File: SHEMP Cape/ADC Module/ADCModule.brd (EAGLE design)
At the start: 48.9 x 67.6 mm, 51 parts, among them U1 ADS8568_PM_64, U2 LP2950-3.3ACZ

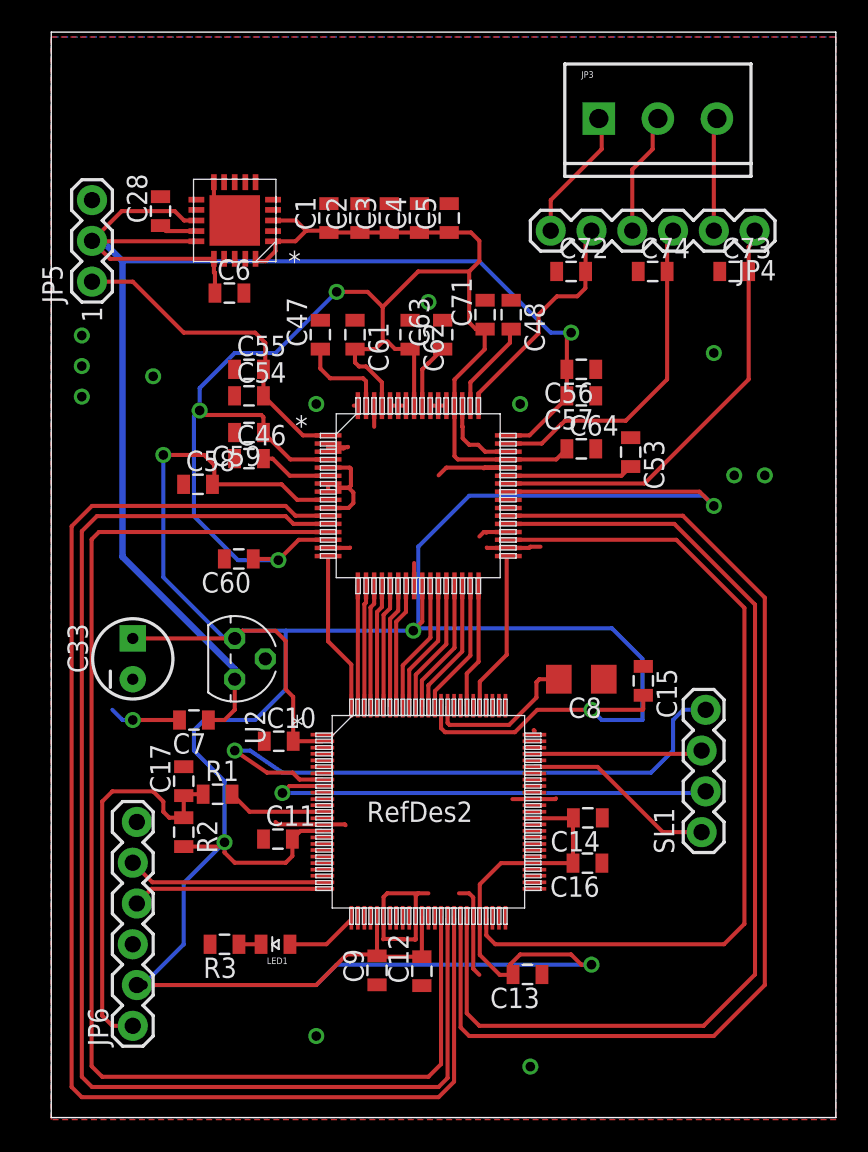
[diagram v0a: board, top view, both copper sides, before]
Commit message: Changed the ADC Module board for boardrouter considerations.
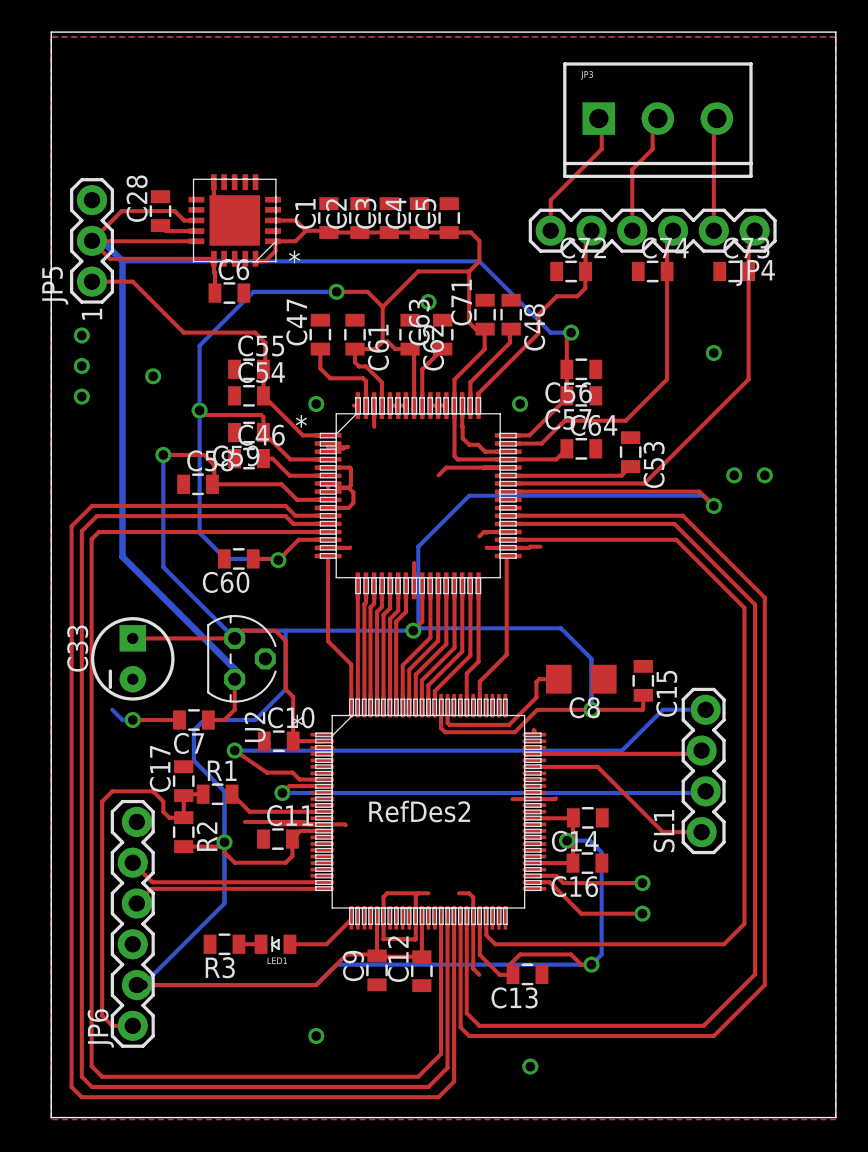
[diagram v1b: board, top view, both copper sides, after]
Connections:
- new net RX1A: U$1.52
- new net TX1A: U$1.53
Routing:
- net RX1A: track 0.00 -> 7.54 mm, vias 0 -> 1
- net TX1A: track 0.00 -> 6.92 mm, vias 0 -> 1
- net GND: track 66.2 -> 71.1 mm
- net VDD3V3_D: track 252.0 -> 248.5 mm, vias 7 -> 8
- net SS: track 38.6 -> 36.5 mm
- net VDD5V0_A: track 104.8 -> 106.4 mm

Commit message: Added new gerbers for boardrouter.
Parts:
- removed JP3: M03SCREW_LOCK, ASL:SCREWTERMINAL-3.5MM-3_LOCK.007S
- added JP1: M03-SCREW-5MM, ASL:SCREWTERMINAL-5MM-3
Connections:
- net N$1: now also JP1.3; no longer JP3.3
- net N$2: now also JP1.2; no longer JP3.2
- net N$3: now also JP1.1; no longer JP3.1
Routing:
- net N$1: track 7.06 -> 8.08 mm
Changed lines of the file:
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@@
 <?xml version="1.0" encoding="utf-8"?>
 <!DOCTYPE eagle SYSTEM "eagle.dtd">
-<eagle version="6.4">
+<eagle version="6.5.0">
 <drawing>
 <settings>
@@
 <element name="C6" library="SensorCape" package="0805" value="10uF" x="11.0998" y="50.0888"/>
 <element name="C7" library="SensorCape" package="0805" value="10uF" x="8.89" y="23.495" rot="R180"/>
-<element name="JP3" library="ASL" package="SCREWTERMINAL-3.5MM-3_LOCK.007S" value="M03SCREW_LOCK" x="34.29" y="60.96"/>
 <element name="JP4" library="ASL" package="1X06" value="" x="37.465" y="53.975" rot="R180"/>
 <element name="U2" library="ASL" package="TO92" value="LP2950-3.3ACZ" x="11.43" y="27.305" rot="R270"/>
@@
 <element name="LED1" library="ASL" package="LED-0805" value="" x="13.97" y="9.525" rot="R180"/>
 <element name="R3" library="SensorCape" package="0805" value="" x="10.795" y="9.525" rot="R180"/>
+<element name="JP1" library="ASL" package="SCREWTERMINAL-5MM-3" value="M03-SCREW-5MM" x="32.385" y="61.595"/>
 </elements>
 <signals>
@@
 </signal>
 <signal name="N$1">
-<contactref element="JP3" pad="3"/>
 <contactref element="JP4" pad="2"/>
-<wire x1="41.275" y1="53.975" x2="41.275" y2="60.7672" width="0.254" layer="1"/>
-<wire x1="41.275" y1="60.7672" x2="41.4678" y2="60.96" width="0.254" layer="1"/>
+<contactref element="JP1" pad="3"/>
+<wire x1="41.275" y1="53.975" x2="41.275" y2="60.485" width="0.4064" layer="16"/>
+<wire x1="41.275" y1="60.485" x2="42.385" y2="61.595" width="0.4064" layer="16"/>
 </signal>
 <signal name="N$2">
-<contactref element="JP3" pad="2"/>
 <contactref element="JP4" pad="4"/>
-<wire x1="36.195" y1="53.975" x2="36.195" y2="57.785" width="0.254" layer="1"/>
-<wire x1="36.195" y1="57.785" x2="37.465" y2="59.055" width="0.254" layer="1"/>
-<wire x1="37.465" y1="59.055" x2="37.465" y2="60.635" width="0.254" layer="1"/>
-<wire x1="37.465" y1="60.635" x2="37.79" y2="60.96" width="0.254" layer="1"/>
+<contactref element="JP1" pad="2"/>
+<wire x1="36.195" y1="53.975" x2="36.195" y2="60.405" width="0.4064" layer="16"/>
+<wire x1="36.195" y1="60.405" x2="37.385" y2="61.595" width="0.4064" layer="16"/>
 </signal>
 <signal name="N$3">
-<contactref element="JP3" pad="1"/>
 <contactref element="JP4" pad="6"/>
-<wire x1="31.115" y1="53.975" x2="31.115" y2="55.88" width="0.254" layer="1"/>
-<wire x1="31.115" y1="55.88" x2="34.29" y2="59.055" width="0.254" layer="1"/>
-<wire x1="34.29" y1="59.055" x2="34.29" y2="60.7822" width="0.254" layer="1"/>
-<wire x1="34.29" y1="60.7822" x2="34.1122" y2="60.96" width="0.254" layer="1"/>
+<contactref element="JP1" pad="1"/>
+<wire x1="31.115" y1="53.975" x2="31.115" y2="60.325" width="0.4064" layer="16"/>
+<wire x1="31.115" y1="60.325" x2="32.385" y2="61.595" width="0.4064" layer="16"/>
 </signal>
 <signal name="N$45">
